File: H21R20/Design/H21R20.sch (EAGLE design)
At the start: 40 parts, among them IC1 ESP32-C3-MINI-1-N4, P1 HEXABIT_17.32_NO_P6, X1 XTALL_CSTCE8M00G52

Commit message: -Changing the MC to STM32G0B1CEU6N -Changing the design of the hardware of the ESP32 circuit and the way it is connected to the MC,and adding test points to help with programming and debugging
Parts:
- removed B, C, D, RX, TX: PAD1, Hexabitz:PAD1
- removed C15: 10uF, HEXABITZ_RCLS:C-0805
- removed C16: 0.1uF, HEXABITZ_RCLS:C-0402
- removed C2: 1.00uF, Hexabitz:C-0805-POL
- removed GND, VDD: PAD4, HEXABITZ_CONNECTION_PARTS:PAD4
- added C11: 47pF, HEXABITZ_RCLS:C-0603
- added C12: 100nF, HEXABITZ_RCLS:C-0603
- added C13: 10uF, HEXABITZ_RCLS:C-1210-POL
- added D+, D-, RX0, TX0: PAD4, HEXABITZ_CONNECTION_PARTS:PAD4
- added D10: RED, HEXABITZ_USER_INTERFACE_PARTS:VLMS1300-GS08
- added D7, D8, D9: BOURNS_CDSOD323-T03SCBOURNS_CDSOD323-T03SC_0_0, HEXABITZ_RCLS:BOURNS_CDSOD323-T03SCBOURNS_CDSOD323-T03SC_0_0
- added JP1: (no value), pinhead:PINHD-1X3
- added Q1: MMBT3904LT1, HEXABITZ_RCLS:MMBT3904LT1
- added R10, R14, R15, R7: 10K, HEXABITZ_RCLS:R-0603
- added R11, R12, R13, R8, R9: 0R, HEXABITZ_RCLS:R-0603
- added R16, R17: 27R, HEXABITZ_RCLS:R-0603
- C1: value 10nF -> 100nF; device Hexabitz:C-0603 -> HEXABITZ_RCLS:C-0603; CAPACITANCE 10nF -> 100nF; MFN KEMET -> AVX CORPORATION; MPN C0603C103K5RACTU -> '0603YC104K4T2A; OCTOPART_URL https://octopart.com/c0603c103k5ractu-kemet-133094?r=sp&s=R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 -> 'https://octopart.com/0603yc104k4t2a-avx+interconnect+%2F+e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; VOLTAGE_RATING 50V -> 16.0 V
- C10: value 0.1uF -> 47pF; device HEXABITZ_RCLS:C-0402 -> HEXABITZ_RCLS:C-0603; CAPACITANCE (none) -> 100nF; MFN (none) -> AVX CORPORATION; MPN (none) -> '0603YC104K4T2A; OCTOPART_URL (none) -> 'https://octopart.com/0603yc104k4t2a-avx+interconnect+%2F+e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; TOLERANCE (none) -> 10%; VOLTAGE_RATING (none) -> 16.0 V
- C3: value 100nF -> 4.7uF; device Hexabitz:C-0603 -> HEXABITZ_RCLS:C-0805-POL; CAPACITANCE 100nF -> 4.7uF; MFN KEMET -> 'Panasonic; MPN C0603C104K8RACTU -> '10TPU4R7MSI; OCTOPART_URL https://octopart.com/c0603c104k8ractu-kemet-145075?r=sp&s=9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 -> https://octopart.com/10tpu4r7msi-panasonic-29487748?r=sp; TOLERANCE 10% -> 20%; VOLTAGE_RATING 10V -> 10.0 V
- C4: value 4.7uF -> 100nF; device Hexabitz:C-0805-POL -> HEXABITZ_RCLS:C-0603; CAPACITANCE 4.7uF -> 100nF; MFN Murata -> AVX CORPORATION; MPN GRM21BC81E475KA12L -> 0603YC104K4T2A; OCTOPART_URL https://octopart.com/grm21bc81e475ka12l-murata-10331911?r=s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 -> 'https://octopart.com/0603yc104k4t2a-avx+interconnect+%2F+e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; VOLTAGE_RATING 25V -> 16.0 V
- C5: device Hexabitz:C-0603 -> HEXABITZ_RCLS:C-0603; MFN KEMET -> AVX CORPORATION; MPN C0603C104K8RACTU -> '0603YC104K4T2A; OCTOPART_URL https://octopart.com/c0603c104k8ractu-kemet-145075?r=sp&s=9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 -> 'https://octopart.com/0603yc104k4t2a-avx+interconnect+%2F+e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; VOLTAGE_RATING 10 -> 16.0 V
- C6: value 100nF -> 1uF; device Hexabitz:C-0603 -> HEXABITZ_RCLS:C-0805-POL; CAPACITANCE 100nF -> 4.7uF; MFN KEMET -> 'YAGEO [VA]; MPN C0603C104K8RACTU -> 'CC0805KKX7R7BB105; OCTOPART_URL https://octopart.com/c0603c104k8ractu-kemet-145075?r=sp&s=9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 -> 'https://octopart.com/cc0805kkx7r7bb105-yageo-8376555?r=sp; TOLERANCE 10% -> 20%; VOLTAGE_RATING 10V -> 10.0 V
- C7: value 4.7uF -> 100nF; device Hexabitz:C-0805-POL -> HEXABITZ_RCLS:C-0603; CAPACITANCE 4.7uF -> 100nF; MFN Murata -> AVX CORPORATION; MPN GRM21BC81E475KA12L -> '0603YC104K4T2A; OCTOPART_URL https://octopart.com/grm21bc81e475ka12l-murata-10331911?r=s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 -> 'https://octopart.com/0603yc104k4t2a-avx+interconnect+%2F+e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; VOLTAGE_RATING 25V -> 16.0 V
- C8: value 100nF -> 4.7uF; device Hexabitz:C-0603 -> HEXABITZ_RCLS:C-0805-POL; CAPACITANCE 100nF -> 1.00uF; MFN KEMET -> 'Panasonic; MPN C0603C104K8RACTU -> '10TPU4R7MSI; OCTOPART_URL https://octopart.com/c0603c104k8ractu-kemet-145075?r=sp&s=9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 -> https://octopart.com/10tpu4r7msi-panasonic-29487748?r=sp; VOLTAGE_RATING 10V -> 16.0 V
- C9: value 100nF -> 1uF; device Hexabitz:C-0603 -> HEXABITZ_RCLS:C-0805-POL; CAPACITANCE 100nF -> 4.7uF; MFN KEMET -> 'YAGEO [VA]; MPN C0603C104K8RACTU -> 'CC0805KKX7R7BB105; OCTOPART_URL https://octopart.com/c0603c104k8ractu-kemet-145075?r=sp&s=9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 -> 'https://octopart.com/cc0805kkx7r7bb105-yageo-8376555?r=sp; TOLERANCE 10V -> 20%; VOLTAGE_RATING 10% -> 10.0 V
- D1: value VLMS1300-GS08 -> RED; device Hexabitz:VLMS1300-GS08 -> HEXABITZ_USER_INTERFACE_PARTS:VLMS1300-GS08; MFN Vishay -> (none); MPN VLMS1300-GS08 -> (none); OCTOPART_URL https://octopart.com/vlms1300-gs08-vishay-21709201?r=sp&s=_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 -> (none)
- D2: value ESD9D5.0ST5G -> BOURNS_CDSOD323-T03SCBOURNS_CDSOD323-T03SC_0_0; device HEXABITZ_RCLS:ESD9D5.0ST5G -> HEXABITZ_RCLS:BOURNS_CDSOD323-T03SCBOURNS_CDSOD323-T03SC_0_0
- D3, D4, D5, D6: value ESD7331MUT5G -> BOURNS_CDSOD323-T03SCBOURNS_CDSOD323-T03SC_0_0; device HEXABITZ_RCLS:ESD7331MUT5G -> HEXABITZ_RCLS:BOURNS_CDSOD323-T03SCBOURNS_CDSOD323-T03SC_0_0
- FB1: value FB-TDK_MMZ1608Y300B -> (none); device Hexabitz:FB-TDK_MMZ1608Y300B -> HEXABITZ_RCLS:FB-TDK_MMZ1608Y300B; MPN MMZ1608Y300B -> MMZ1608Y300BTA00; OCTOPART_URL https://octopart.com/mmz1608y300b-tdk-368280?r=sp&s=cd9_2ZE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 -> https://octopart.com/mmz1608y300bta00-tdk-7906990?r=sp
- P1: value HEXABIT_17.32_NO_P6 -> HEXABIT_17.32_NO_P6_P7_P12; device hexabitz_connectors:HEXABIT_17.32_NO_P6 -> hexabitz_connectors:HEXABIT_17.32_NO_P6_P7_P12
- R: value PAD1 -> (none); device Hexabitz:PAD1 -> HEXABITZ_USER_INTERFACE_PARTS:PINHD-1X1
- R1: value 270.0R -> 270R; device Hexabitz:R-0603 -> HEXABITZ_RCLS:R-0603; MFN Yageo -> 'Panasonic; MPN RC0603FR-07270RL -> 'ERJ-3GEYJ271V; OCTOPART_URL https://octopart.com/search?q=RC0603FR-07270RL&start=0 -> https://octopart.com/erj-3geyj271v-panasonic-55560546?r=sp; RESISTANCE 270.0 Ohm -> 270R; TOLERANCE 5% -> (none)
- R2: value 0.0R -> 10K; device Hexabitz:R-0603 -> HEXABITZ_RCLS:R-0603; MFN Yageo -> Vishay; MPN RC0603JR-070RL -> '060300J0103T5E; OCTOPART_URL https://octopart.com/rc0603jr-070rl-yageo-1241539?r=sp&s=X2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 -> https://octopart.com/search?q=060300J0103T5E&currency=USD&s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; RESISTANCE 0.0 Ohm -> 10K
- R3: value 10.0K -> 0.0R; device Hexabitz:R-0603 -> HEXABITZ_RCLS:R-0603; MFN Yageo -> YAGEO [VR]; MPN RC0603JR-0710KL -> RC0603JR-070RL; OCTOPART_URL https://octopart.com/search?q=RC0603JR-0710KL&start=0 -> https://octopart.com/rc0603jr-070rl-yageo-1241539?r=sp; RESISTANCE 10.0K Ohm -> 0R; TOLERANCE 5% -> (none)
- R4: value 10k -> 270R; device HEXABITZ_RCLS:R-0402 -> HEXABITZ_RCLS:R-0603; MFN (none) -> 'Panasonic; MPN (none) -> 'ERJ-3GEYJ271V; OCTOPART_URL (none) -> https://octopart.com/erj-3geyj271v-panasonic-55560546?r=sp; RESISTANCE (none) -> 270R
- R5: value 100R -> 10K; device HEXABITZ_RCLS:R-0402 -> HEXABITZ_RCLS:R-0603; MFN (none) -> YAGEO [VR]; MPN (none) -> RC0603JR-070RL; OCTOPART_URL (none) -> https://octopart.com/rc0603jr-070rl-yageo-1241539?r=sp; RESISTANCE (none) -> 0R
- U1: value (none) -> STM32G0B1CEU6NUFQFPN48_STM32_STM; device Hexabitz:STM32F091CBU6 -> HEXABITZ_ICs:STM32G0B1CEU6NUFQFPN48_STM32_STM; OCTOPART_URL (none) -> https://octopart.com/stm32g0b1ceu6n-stmicroelectronics-1163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
- X1: device Hexabitz:XTALL_CSTCE8M00G52 -> HEXABITZ_OTHER_PARTS:XTALL_CSTCE8M00G52; MPN (none) -> CSTNE8M00G550000R0; OCTOPART_URL (none) -> https://octopart.com/cstne8m00g550000r0-murata-91406934?r=sp
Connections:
- net UART1_RX renamed USART1_RX
- net UART1_TX renamed USART1_TX
- net UART2_RX renamed USART2_RX
- net UART2_TX renamed USART2_TX
- net UART3_RX renamed USART3_RX
- net UART3_TX renamed USART3_TX
- net UART4_RX renamed USART4_RX
- net UART4_TX renamed USART4_TX
- removed net B1: B.P$1, R3.2, U1.PF11-OSC_BOOT0
- removed net CHIP_EN: C10.1, IC1.EN, R4.1, U1.PA8
- removed net ESP_BOOT: IC1.IO9, U1.PA6
- removed net ESP_MODE: IC1.IO8, U1.PA7
- removed net N$1 (its old number): D3.2, IC1.IO4, TMS.P$1
- removed net N$2 (its old number): D4.2, IC1.IO5, TDI.P$1
- removed net R1: C8.1, R.P$1, U1.NRST
- removed net UART5_RX: IC1.RXD0, RX.P$1, U1.PB4
- removed net UART5_TX: IC1.TXD0, TX.P$1, U1.PB3
- removed net UART6_RX: P1.SD3, U1.PA5
- removed net UART6_TX: P1.SU3, U1.PA4
- new net C: JP1.1, JP1.2, R2.2, U1.PA14-BOOT0
- new net D: JP1.3, U1.PA13
- new net DATA_N: C11.2, IC1.IO18, R16.1
- new net DATA_P: C10.2, IC1.IO19, R17.1
- new net D_N: D-.P$1, D6.2, R16.2
- new net D_P: D+.P$1, D7.2, R17.2
- new net ESP32_BOOT: IC1.IO9, U1.PC13
- new net ESP32_CS: IC1.IO1, U1.PD0
- new net ESP32_MISO: R13.2, U1.PB6
- new net ESP32_MOSI: R12.2, U1.PB7
- new net ESP32_RESET: R15.1, U1.PA15
- new net ESP32_RX0: R8.2, U1.PB8
- new net ESP32_SCK: R11.2, U1.PD1
- new net ESP32_TX0: R9.2, U1.PB9
- new net N$12: C4.2, R.1, U1.PF2-NRST
- new net N$13: Q1.B, R15.2
- new net N$14: D10.A, IC1.IO3
- new net N$15: IC1.IO2, R5.1
- new net N$17: R1.2, U1.PB14
- new net N$25: C9.+, IC1.EN, Q1.C, R14.2
- new net N$4: IC1.IO8, R7.1
- new net N$5: D10.C, R4.2
- new net N$6: D8.2, IC1.RXD0, R8.1, RX0.P$1
- new net USART5_RX: P1.SD3, U1.PB1
- new net USART5_TX: P1.SU3, U1.PB0
- net GND: now also C10.1, C11.1, C12.1, C13.-, C4.1, C7.1, C8.-, C9.-, D2.1, D7.1, D8.1, D9.1, Q1.E, R10.2, R4.1, U1.EPAD, U1.PB12, U1.PB13, U1.VSS; no longer C10.2, C15.2, C16.2, C3.2, C4.-, C5.2, C6.2, C7.-, C8.2, C9.2, D2.2, GND.P$1, P1.GND1, P1.GND6, R5.1, U1.EP, U1.VSS_0, U1.VSS_1, U1.VSS_2
- net N$10: now also D3.2, R11.1; no longer D6.2
- net N$11: now also D5.2, IC1.IO5, R13.1, TDI.P$1; no longer IC1.IO10, R5.2
- net N$3: now also D4.2, IC1.IO4, TMS.P$1; no longer R1.2, U1.PA11
- net N$7: now also D9.2, IC1.TXD0, R9.1, TX0.P$1; no longer D.P$1, U1.PA13
- net N$8: now also D2.2, R12.1; no longer D5.2
- net N$9: now also IC1.IO10, R10.1; no longer C.P$1, U1.PA14
- net VDD: now also C12.2, C13.+, C7.2, C8.+, FB1.1, R14.1, R5.2, R7.2; no longer C15.1, C16.1, C3.1, C4.+, C5.1, C6.1, C7.+, C9.1, D2.1, FB1.2, P1.VDD1, P1.VDD6, R4.2, U1.VBAT, U1.VDD_0, U1.VDD_1, VDD.P$1
- net VDDA: now also C1.2, C3.+, C5.2, C6.+, FB1.2, U1.VBAT, U1.VDD/VDDA, U1.VREF+; no longer C1.1, C2.+, FB1.1, U1.VDDA
- net VSSA: now also C1.1, C3.-, C5.1, C6.-, R3.2, U1.VSS/VSSA; no longer C1.2, C2.-, R2.2, U1.VSS_A
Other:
- note added: "B"
- note added: "ESP32-C3 Wifi+BLE"
- note added: "H21R20"
- note added: "H21R20_Backend"
- note added: "H21R20_Frontend"
- note added: "Ibrahim Zaeiter"
- note added: "SPI2"
- note added: "To use external USB to FTDI desolder R8 & R9"
- note added: "To use external USB to JTAG debugger desolder R11 & R12 & R13"
- note added: "USART6"
- note added: "VDD\\\VDDA Coupling"
- note added: "Vref Coupling"
- note removed: "Anas Kaadan"
- note removed: "ESP32-C3 WiFi+BLE"
- note removed: "H21R2"
- note removed: "H21R2_Backend"
- note removed: "H21R2_Frontend"
- note removed: "VBAT"
- note removed: "VDD Coupling"
- note removed: "VDDA Coupling"

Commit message: -Changing some issues in the design to improve the performance
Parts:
- removed C9: 1uF, HEXABITZ_RCLS:C-0805-POL
- removed Q1: MMBT3904LT1, HEXABITZ_RCLS:MMBT3904LT1
- removed R15: 10K, HEXABITZ_RCLS:R-0603
- added C2: 100nF, HEXABITZ_RCLS:C-0603
- X1: value XTALL_CSTCE8M00G52 -> 8MHZ
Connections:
- removed net N$11 (its old number): D5.2, IC1.IO5, R13.1, TDI.P$1
- removed net N$13: Q1.B, R15.2
- removed net N$25: C9.+, IC1.EN, Q1.C, R14.2
- removed net N$8: D2.2, IC1.IO6, R12.1, TCK.P$1
- removed net USART3_RX: P1.SD4, U1.PB11
- removed net USART3_TX: P1.SU4, U1.PB10
- new net N$10: D2.2, IC1.IO6, R13.1, TCK.P$1
- new net N$18: D5.2, IC1.IO5, R12.1, TDI.P$1
- new net USART6_RX: P1.SD3, U1.PA5
- new net USART6_TX: P1.SU3, U1.PA4
- net ESP32_CS: now also U1.PA15; no longer U1.PD0
- net ESP32_MISO: now also U1.PB4; no longer U1.PB6
- net ESP32_MOSI: now also U1.PB5; no longer U1.PB7
- net ESP32_RESET: now also C2.2, IC1.EN, R14.2, U1.PD0; no longer R15.1, U1.PA15
- net ESP32_SCK: now also U1.PB3; no longer U1.PD1
- net GND: now also C2.1, U1.PB11, U1.PC14-OSC32_IN, U1.PC15-OSC32_OUT; no longer C9.-, Q1.E
- net N$6: now also D9.2; no longer D8.2
- net N$7: now also D8.2; no longer D9.2
- net USART1_RX: now also P1.SD4; no longer P1.SD5
- net USART1_TX: now also P1.SU4; no longer P1.SU5
- net USART5_RX: now also P1.SD5, U1.PD2; no longer P1.SD3, U1.PB1
- net USART5_TX: now also P1.SU5, U1.PD3; no longer P1.SU3, U1.PB0
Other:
- note added: "ESP32_USART0"
- note added: "SPI1 ,SPI3"
- note added: "USART3"
- note added: "USB"
- note removed: "SPI2"
- note removed: "USART6"
- moved on the sheet: C1, C10, C11, C12, C13, C3, C4, C5, C6, C7, C8, D+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

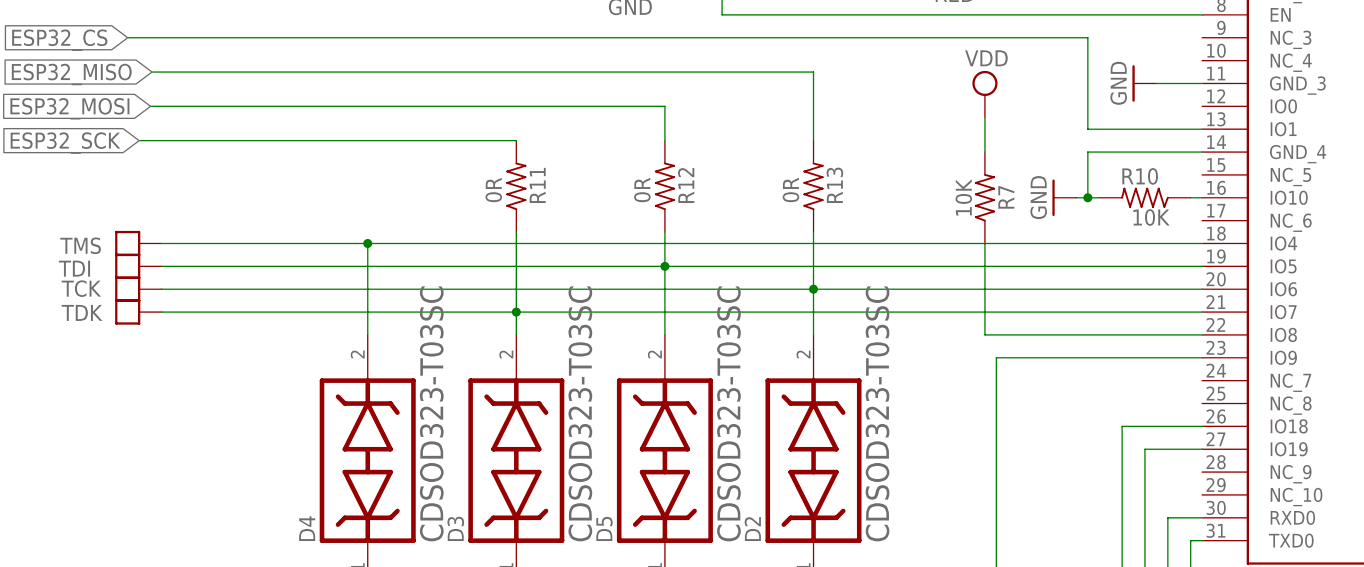
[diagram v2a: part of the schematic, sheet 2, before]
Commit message: -Changing the placement of the ESP32
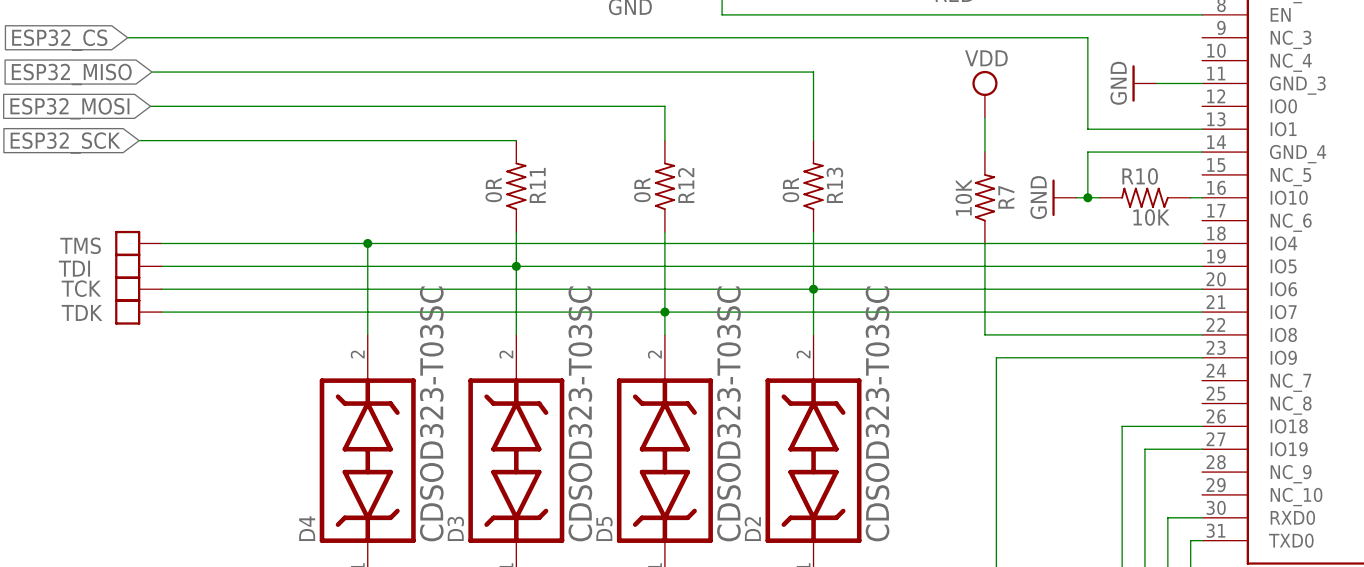
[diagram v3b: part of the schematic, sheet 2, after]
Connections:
- net N$11: now also D5.2, R12.1; no longer D3.2, R11.1
- net N$18: now also D3.2, R11.1; no longer D5.2, R12.1
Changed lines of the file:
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@@
 <part name="SUPPLY12" library="supply2" library_urn="urn:adsk.eagle:library:372" deviceset="VCC" device="" value="VDDA"/>
 <part name="SUPPLY9" library="supply2" library_urn="urn:adsk.eagle:library:372" deviceset="GND1" device="" value="VSSA"/>
-<part name="U1" library="HEXABITZ_ICs" library_urn="urn:adsk.eagle:library:20064554" deviceset="STM32G0B1CEU6N" device="UFQFPN48_STM32_STM" package3d_urn="urn:adsk.eagle:package:33906703/3">
+<part name="U1" library="HEXABITZ_ICs" library_urn="urn:adsk.eagle:library:20064554" deviceset="STM32G0B1CEU6N" device="UFQFPN48_STM32_STM" package3d_urn="urn:adsk.eagle:package:33906703/4">
 <attribute name="OCTOPART_URL" value="https://octopart.com/stm32g0b1ceu6n-stmicroelectronics-116364672?r=sp"/>
 </part>
 <part name="R" library="HEXABITZ_USER_INTERFACE_PARTS" library_urn="urn:adsk.eagle:library:20064563" deviceset="PINHD-1X1" device="" package3d_urn="urn:adsk.eagle:package:22485/2"/>
 <part name="JP1" library="pinhead" deviceset="PINHD-1X3" device="" package3d_urn="urn:adsk.eagle:package:22458/2"/>
-<part name="IC1" library="HEXABITZ_ICs" library_urn="urn:adsk.eagle:library:20064554" deviceset="ESP32-C3-MINI-1-N4" device="" package3d_urn="urn:adsk.eagle:package:28470191/1"/>
+<part name="IC1" library="HEXABITZ_ICs" library_urn="urn:adsk.eagle:library:20064554" deviceset="ESP32-C3-MINI-1-N4" device="" package3d_urn="urn:adsk.eagle:package:28470191/2"/>
 <part name="GND1" library="supply1" library_urn="urn:adsk.eagle:library:371" deviceset="GND" device=""/>
 <part name="GND10" library="supply1" library_urn="urn:adsk.eagle:library:371" deviceset="GND" device=""/>
@@
 <net name="N$10" class="0">
 <segment>
-<pinref part="R13" gate="G$1" pin="1"/>
-<pinref part="D2" gate="G$0" pin="2"/>
 <pinref part="TCK" gate="G$1" pin="P$1"/>
-<wire x1="156.21" y1="133.35" x2="156.21" y2="128.27" width="0.1524" layer="91"/>
-<wire x1="83.82" y1="133.35" x2="156.21" y2="133.35" width="0.1524" layer="91"/>
 <pinref part="IC1" gate="G$1" pin="IO6"/>
-<junction x="156.21" y="133.35"/>
+<wire x1="83.82" y1="133.35" x2="156.21" y2="133.35" width="0.1524" layer="91"/>
+<pinref part="R13" gate="G$1" pin="1"/>
 <wire x1="156.21" y1="133.35" x2="199.39" y2="133.35" width="0.1524" layer="91"/>
 <wire x1="156.21" y1="139.7" x2="156.21" y2="133.35" width="0.1524" layer="91"/>
+<junction x="156.21" y="133.35"/>
+<pinref part="D2" gate="G$0" pin="2"/>
+<wire x1="156.21" y1="128.27" x2="156.21" y2="133.35" width="0.1524" layer="91"/>
 </segment>
 </net>
 <net name="N$11" class="0">
 <segment>
-<pinref part="R11" gate="G$1" pin="1"/>
-<wire x1="123.19" y1="139.7" x2="123.19" y2="130.81" width="0.1524" layer="91"/>
-<pinref part="D3" gate="G$0" pin="2"/>
 <pinref part="TDK" gate="G$1" pin="P$1"/>
-<wire x1="123.19" y1="130.81" x2="123.19" y2="128.27" width="0.1524" layer="91"/>
-<wire x1="83.82" y1="130.81" x2="123.19" y2="130.81" width="0.1524" layer="91"/>
+<wire x1="83.82" y1="130.81" x2="139.7" y2="130.81" width="0.1524" layer="91"/>
 <pinref part="IC1" gate="G$1" pin="IO7"/>
-<wire x1="199.39" y1="130.81" x2="123.19" y2="130.81" width="0.1524" layer="91"/>
-<junction x="123.19" y="130.81"/>
+<pinref part="R12" gate="G$1" pin="1"/>
+<wire x1="139.7" y1="130.81" x2="199.39" y2="130.81" width="0.1524" layer="91"/>
+<wire x1="139.7" y1="139.7" x2="139.7" y2="130.81" width="0.1524" layer="91"/>
+<junction x="139.7" y="130.81"/>
+<pinref part="D5" gate="G$0" pin="2"/>
+<wire x1="139.7" y1="128.27" x2="139.7" y2="130.81" width="0.1524" layer="91"/>
 </segment>
 </net>
 <net name="N$18" class="0">
 <segment>
-<pinref part="R12" gate="G$1" pin="1"/>
 <pinref part="TDI" gate="G$1" pin="P$1"/>
 <pinref part="IC1" gate="G$1" pin="IO5"/>
-<wire x1="83.82" y1="135.89" x2="139.7" y2="135.89" width="0.1524" layer="91"/>
-<pinref part="D5" gate="G$0" pin="2"/>
-<junction x="139.7" y="135.89"/>
-<wire x1="139.7" y1="135.89" x2="199.39" y2="135.89" width="0.1524" layer="91"/>
-<wire x1="139.7" y1="135.89" x2="139.7" y2="128.27" width="0.1524" layer="91"/>
-<wire x1="139.7" y1="139.7" x2="139.7" y2="135.89" width="0.1524" layer="91"/>
+<wire x1="83.82" y1="135.89" x2="123.19" y2="135.89" width="0.1524" layer="91"/>
+<pinref part="D3" gate="G$0" pin="2"/>
+<wire x1="123.19" y1="135.89" x2="199.39" y2="135.89" width="0.1524" layer="91"/>
+<wire x1="123.19" y1="128.27" x2="123.19" y2="135.89" width="0.1524" layer="91"/>
+<junction x="123.19" y="135.89"/>
+<pinref part="R11" gate="G$1" pin="1"/>
+<wire x1="123.19" y1="139.7" x2="123.19" y2="135.89" width="0.1524" layer="91"/>
 </segment>
 </net>

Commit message: -Correcting some documentaion issues
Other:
- note added: "To use external FTDI desolder R8 & R9"
- note added: "To use external JTAG debugger desolder R11 & R12 & R13"
- note removed: "To use external USB to FTDI desolder R8 & R9"
- note removed: "To use external USB to JTAG debugger desolder R11 & R12 & R13"
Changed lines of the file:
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@@
 <?xml version="1.0" encoding="utf-8"?>
 <!DOCTYPE eagle SYSTEM "eagle.dtd">
-<eagle version="9.6.2">
+<eagle version="9.6.1">
 <drawing>
 <settings>
@@
 <text x="242.57" y="6.35" size="1.9304" layer="100" font="vector">www.hexabitz.com</text>
 <text x="180.34" y="5.08" size="1.9304" layer="101" font="vector">Ibrahim Zaeiter</text>
-<text x="35.56" y="154.94" size="1.778" layer="102" align="center">To use external USB to JTAG debugger
+<text x="35.56" y="154.94" size="1.778" layer="102" align="center">To use external JTAG debugger
  desolder R11 &amp; R12 &amp; R13</text>
-<text x="43.18" y="53.34" size="1.778" layer="102" rot="R180" align="center">To use external USB to FTDI
+<text x="43.18" y="53.34" size="1.778" layer="102" rot="R180" align="center">To use external FTDI
  desolder R8 &amp; R9</text>
 <wire x1="76.2" y1="86.36" x2="74.93" y2="86.36" width="0.1524" layer="102"/>
